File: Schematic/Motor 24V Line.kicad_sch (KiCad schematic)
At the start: 35 parts, among them Q31 CSD19531Q5A, Q32 CSD19531Q5A, U12 LM25190RGYR

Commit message: 1st Schematic Review
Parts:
- renumbered C137 to C140, C138 to C141, C139 to C142, C140 to C143, C141 to C144, C142 to C145, C143 to C146, C144 to C147, C145 to C148, C146 to C149, C147 to C150, C148 to C151, C149 to C152, C150 to C153, C151 to C154, C152 to C155, C153 to C156, C154 to C157, C155 to C158, C156 to C159, C157 to C160, C158 to C161, R129 to R131, R130 to R132, R131 to R133, R132 to R134, R133 to R135, R134 to R136, R135 to R137, R136 to R138, U12 to U15

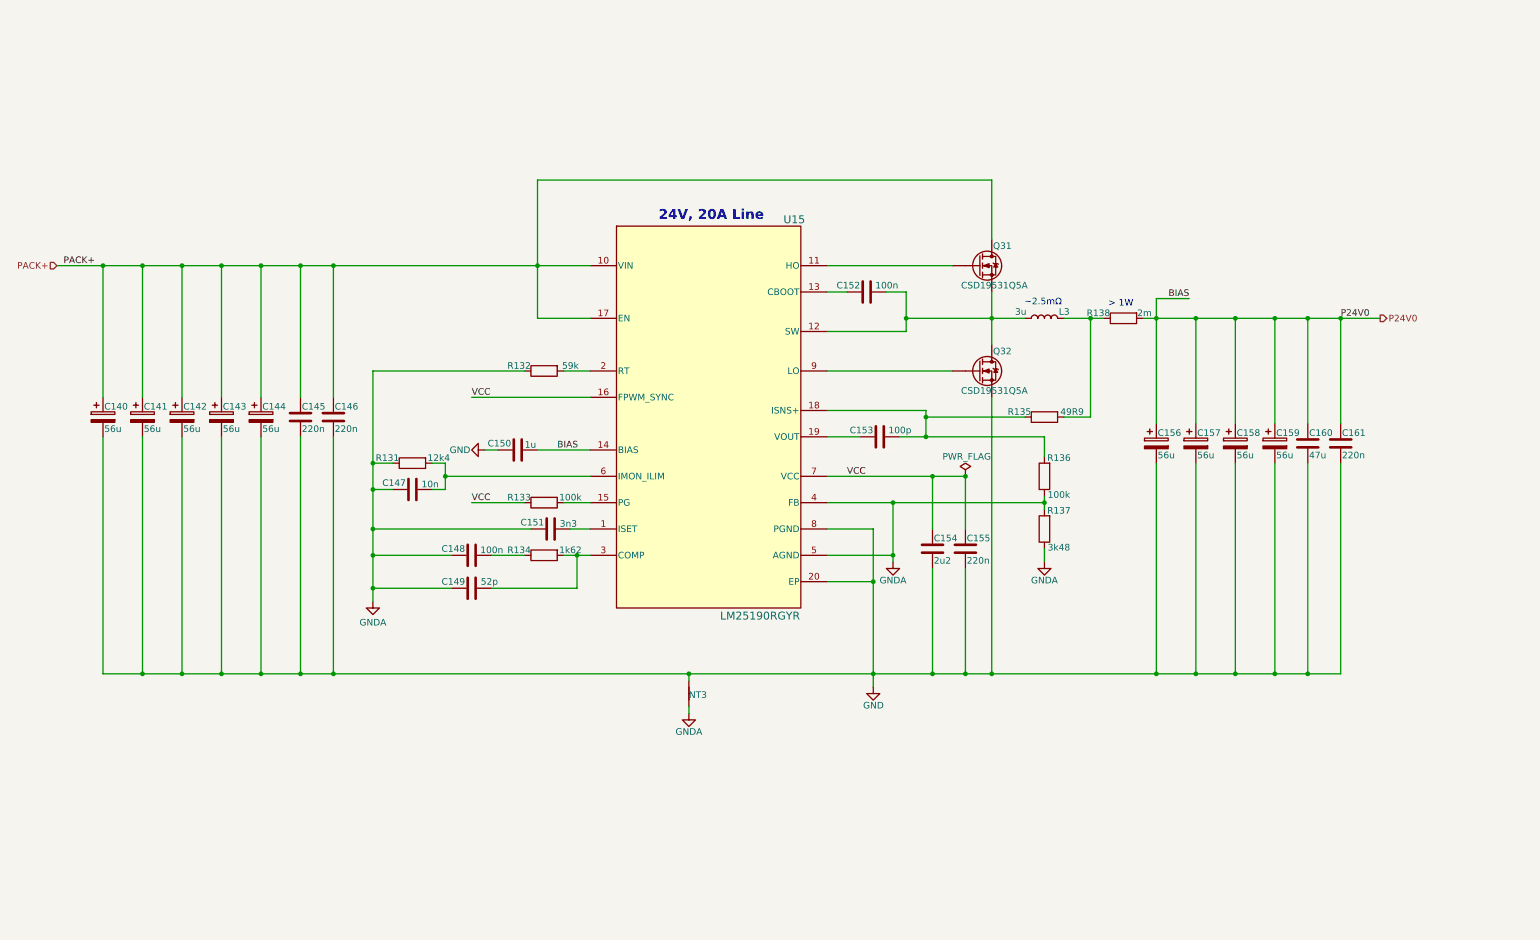
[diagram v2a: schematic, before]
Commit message: fixed power lines
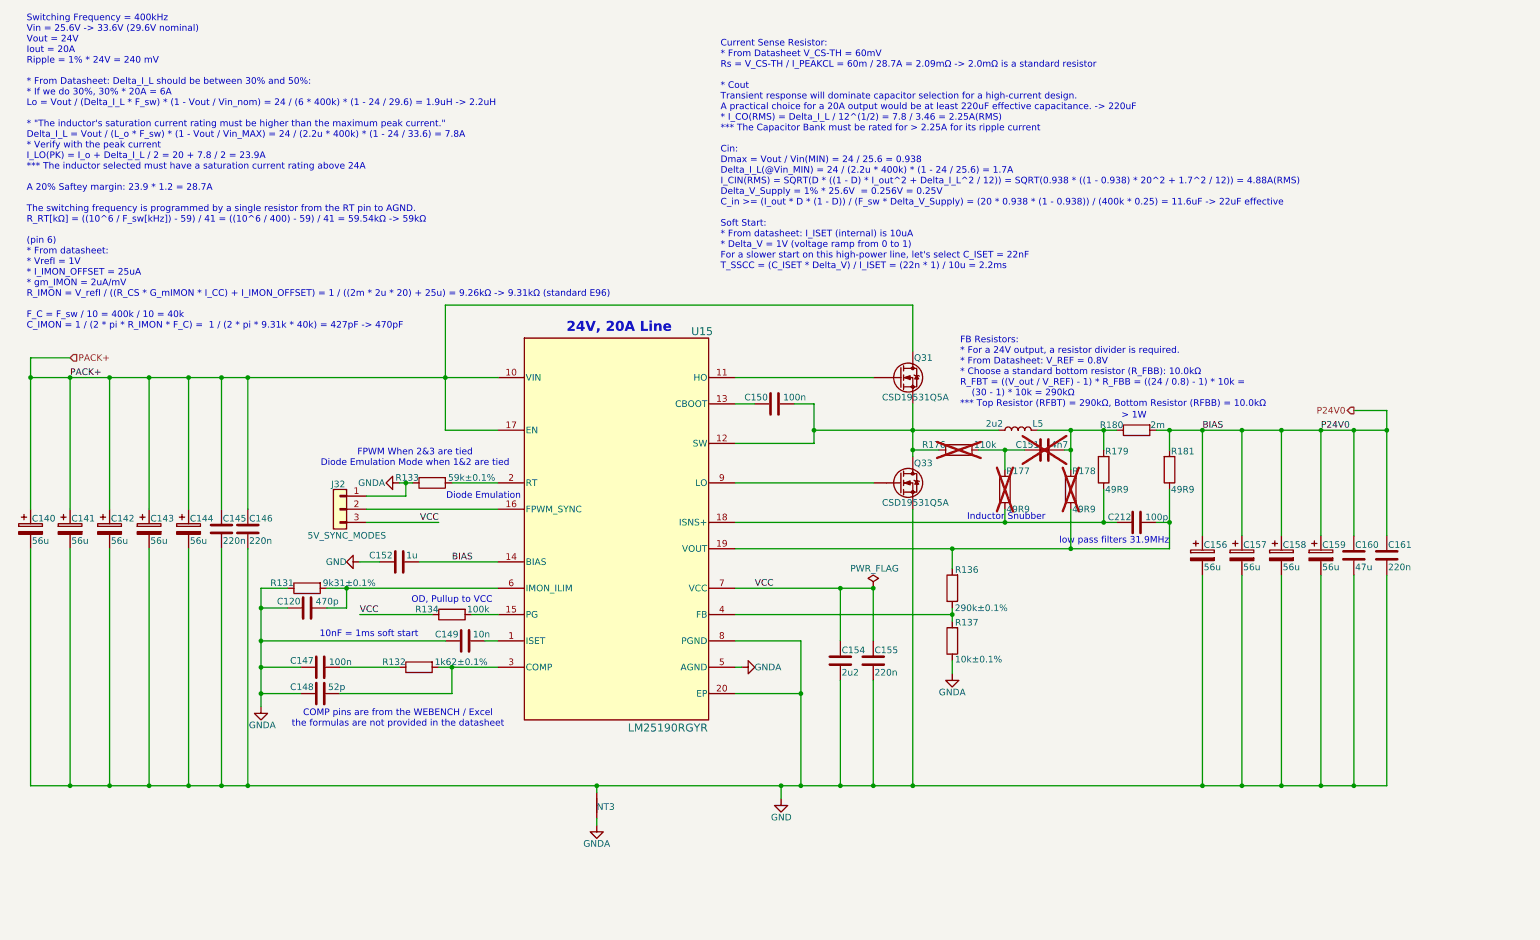
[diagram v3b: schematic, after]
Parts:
- removed C153: 100p, symbol Device:C
- removed L3: 3u, symbol Device:L
- removed Q32: CSD19531Q5A, Package_TO_SOT_SMD:TDSON-8-1, symbol Transistor_FET:CSD19531Q5A
- removed R135: 49R9, symbol Device:R
- removed R138: 2m, symbol Device:R
- added C120: 470p, symbol Device:C
- added C212: 100p, symbol Device:C
- added J32: 5V_SYNC_MODES, symbol Connector_Generic:Conn_01x03
- added L5: 2u2, symbol Device:L
- added Q33: CSD19531Q5A, Package_TO_SOT_SMD:TDSON-8-1, symbol Transistor_FET:CSD19531Q5A
- added R176: 110k, symbol Device:R
- added R177, R178, R179, R181: 49R9, symbol Device:R
- added R180: 2m, symbol Device:R
- C147: value 10n -> 100n
- C148: value 100n -> 52p
- C149: value 52p -> 10n
- C150: value 1u -> 100n
- C151: value 3n3 -> 4n7; now not fitted
- C152: value 100n -> 1u
- R131: value 12k4 -> 9k31±0.1%
- R132: value 59k -> 1k62±0.1%
- R133: value 100k -> 59k±0.1%
- R134: value 1k62 -> 100k
- R136: value 100k -> 290k±0.1%
- R137: value 3k48 -> 10k±0.1%
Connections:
- net GND: now also C152.1, Q33.1 (S), Q33.2 (S), Q33.3 (S); no longer C150.1
- net GNDA: now also R133.1, C120.1, J32.1 (Pin_1); no longer C151.1, R132.1, R136.1, R137.2, U15.4 (FB)
- net P24V0: now also C152.2, R180.2, R181.2; no longer C150.2
- net VCC: now also R134.1, J32.3 (Pin_3); no longer R133.1, U15.16 (FPWM_SYNC)
- net at Q31.1 (S), Q31.2 (S), Q31.3 (S)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: now also C150.2, L5.1, Q33.5 (D), R176.1; no longer C152.2
- net at U15.18 (ISNS+): now also C212.1, R177.1, R179.1; no longer R136.2
- net at C148.2: now also R132.2, U15.3 (COMP); no longer R134.1
- net at U15.19 (VOUT): now also R136.2, C212.2, R178.1, R181.1
- net at R133.2: now also U15.2 (RT); no longer U15.15 (PG)
- net at C151.2: now also L5.2, R178.2, R179.2, R180.1; no longer U15.1 (ISET)
- net at U15.13 (CBOOT): now also C150.1; no longer C152.1
- net at R131.2, U15.6 (IMON_ILIM): now also C120.2; no longer C147.2
- net at U15.9 (LO): now also Q33.4 (G)
- new net: C147.2, R132.1
- new net: C151.1, R176.2, R177.2
- new net: C149.2, U15.1 (ISET)
- new net: R134.2, U15.15 (PG)
- new net: J32.2 (Pin_2), U15.16 (FPWM_SYNC)
- new net: R136.1, R137.2, U15.4 (FB)
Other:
- note added: "10nF = 1ms soft start"
- note added: "COMP pins are from the WEBENCH / Excel the formulas are not provided in the datasheet"
- note added: "Current Sense Resistor: * From Datasheet V_CS-TH = 60mV Rs = V_CS-TH / I_PEAKCL = 60m / 28.7A = 2.09mΩ -> 2.0mΩ is a standard resistor * Cout Transient response will dominate capacitor selection for a high-current design. A practical choice for a 20A output would be at least 220uF effective capacitance. -> 220uF * I_CO(RMS) = Delta_I_L / 12^(1/2) = 7.8 / 3.46 = 2.25A(RMS) *** The Capacitor Bank m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"
- note added: "Diode Emulation"
- note added: "FB Resistors: * For a 24V output, a resistor divider is required. * From Datasheet: V_REF = 0.8V * Choose a standard bottom resistor (R_FBB): 10.0kΩ R_FBT = ((V_out / V_REF) - 1) * R_FBB = ((24 / 0.8) - 1) * 10k = (30 - 1) * 10k = 290kΩ *** Top Resistor (RFBT) = 290kΩ, Bottom Resistor (RFBB) = 10.0kΩ"
- note added: "FPWM When 2&3 are tied Diode Emulation Mode when 1&2 are tied"
- note added: "Inductor Snubber"
- note added: "OD, Pullup to VCC"
- note added: "Switching Frequency = 400kHz Vin = 25.6V -> 33.6V (29.6V nominal) Vout = 24V Iout = 20A Ripple = 1% * 24V = 240 mV * From Datasheet: Delta_I_L should be between 30% and 50%: * If we do 30%, 30% * 20A = 6A Lo = Vout / (Delta_I_L * F_sw) * (1 - Vout / Vin_nom) = 24 / (6 * 400k) * (1 - 24 / 29.6) = 1.9uH -> 2.2uH * "The inductor's saturation current rating must be higher than the maximum peak curren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"
- note added: "low pass filters 31.9MHz"
- note removed: "~2.5mΩ"
- moved on the sheet: C140, C141, C142, C143, C144, C145, C146, C154, C155, C156, C157, C158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

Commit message: updates
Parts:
- renumbered C140 to C141, C141 to C142, C142 to C143, C143 to C144, C144 to C145, C145 to C146, C146 to C147, C120 to C148, C147 to C149, C148 to C150, C152 to C151, C149 to C152, C150 to C153, C151 to C156, C212 to C157, C156 to C158, C157 to C159, C158 to C160, C159 to C161, C160 to C162, C161 to C163, J32 to J11, L5 to L3, Q33 to Q32, R131 to R140, R132 to R141, R133 to R142, R134 to R143, R136 to R144, R137 to R145, R176 to R146, R177 to R147, R178 to R148, R179 to R149, R180 to R150, R181 to R151
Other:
- note added: "using global GNDA, is this what we should be doing?"
- moved on the sheet: C147

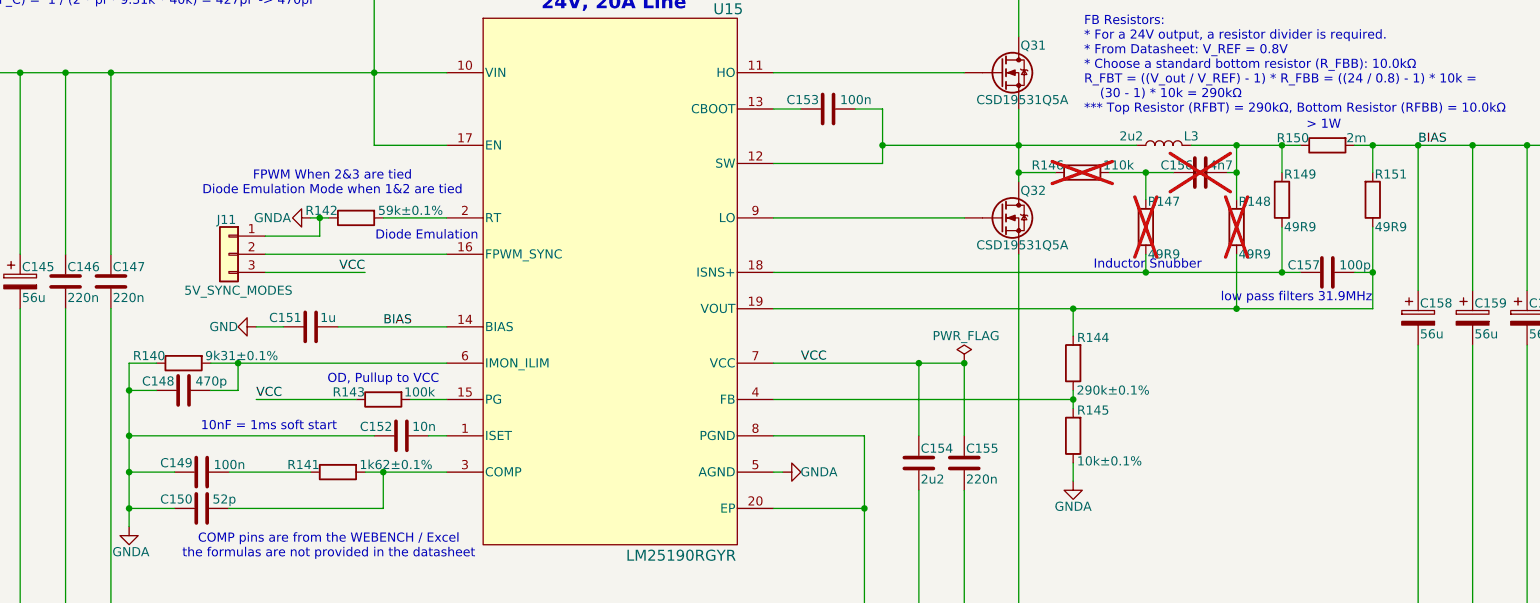
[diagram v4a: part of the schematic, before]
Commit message: updated fuel guage
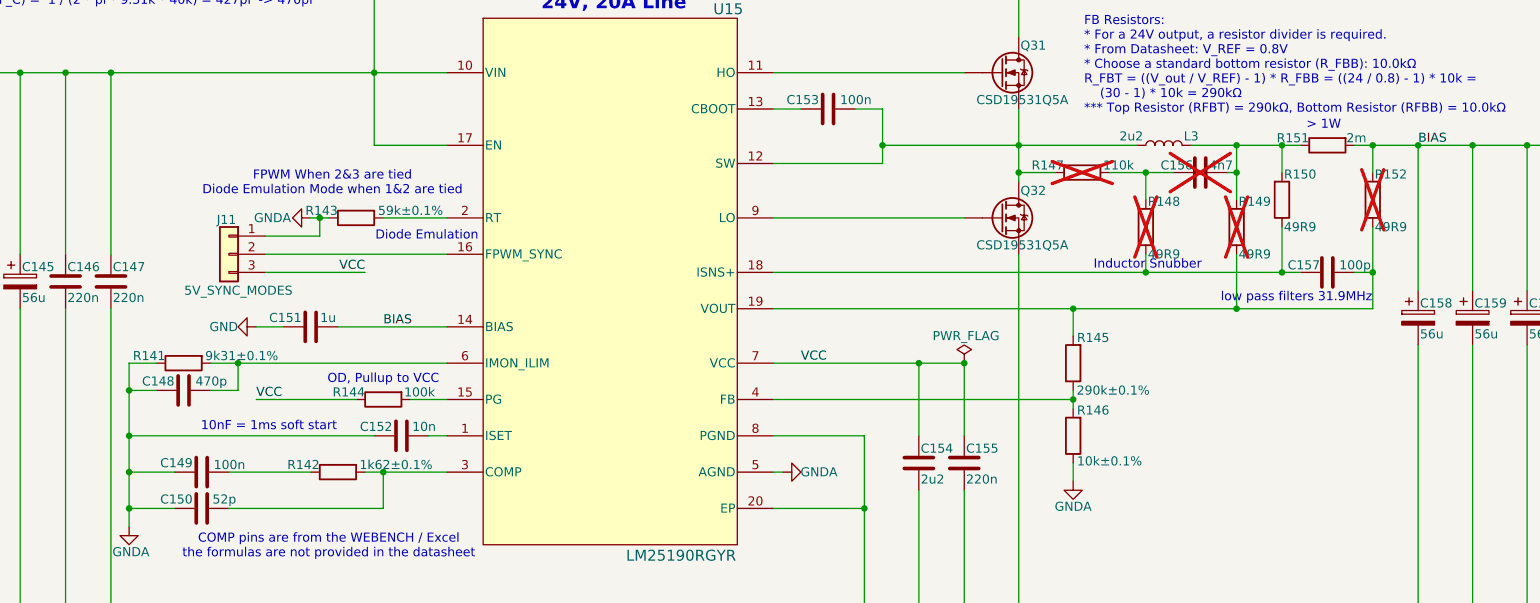
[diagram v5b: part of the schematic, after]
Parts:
- R152: renamed from R151; now not fitted
- renumbered R140 to R141, R141 to R142, R142 to R143, R143 to R144, R144 to R145, R145 to R146, R146 to R147, R147 to R148, R148 to R149, R149 to R150, R150 to R151
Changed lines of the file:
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@@
 		(on_board yes)
 		(dnp no)
-		(property "Reference" "R142"
+		(property "Reference" "R143"
 			(at 89.154 104.394 90)
 			(effects
@@
 			(project "STAR"
 				(path "/fc8533bc-25dd-4c20-9b4c-ffebebd6739b/f73d6367-f3ba-42df-a3ea-bd155f1c219f/3f0d1238-5e65-4d96-8961-a5c2e74dde4b"
-					(reference "R142")
+					(reference "R143")
 					(unit 1)
 				)
@@
 		(on_board yes)
 		(dnp yes)
-		(property "Reference" "R147"
+		(property "Reference" "R148"
 			(at 207.01 103.124 0)
 			(effects
@@
 			(project "STAR"
 				(path "/fc8533bc-25dd-4c20-9b4c-ffebebd6739b/f73d6367-f3ba-42df-a3ea-bd155f1c219f/3f0d1238-5e65-4d96-8961-a5c2e74dde4b"
-					(reference "R147")
+					(reference "R148")
 					(unit 1)
 				)
@@
 		(on_board yes)
 		(dnp no)
-		(property "Reference" "R141"
+		(property "Reference" "R142"
 			(at 86.614 139.954 90)
 			(effects
@@
 			(project "STAR"
 				(path "/fc8533bc-25dd-4c20-9b4c-ffebebd6739b/f73d6367-f3ba-42df-a3ea-bd155f1c219f/3f0d1238-5e65-4d96-8961-a5c2e74dde4b"
-					(reference "R141")
+					(reference "R142")
 					(unit 1)
 				)
@@
 		(in_bom yes)
 		(on_board yes)
-		(dnp no)
-		(property "Reference" "R151"
+		(dnp yes)
+		(property "Reference" "R152"
 			(at 238.76 99.314 0)
 			(effects
@@
 			(project "STAR"
 				(path "/fc8533bc-25dd-4c20-9b4c-ffebebd6739b/f73d6367-f3ba-42df-a3ea-bd155f1c219f/3f0d1238-5e65-4d96-8961-a5c2e74dde4b"
-					(reference "R151")
+					(reference "R152")
 					(unit 1)
 				)
@@
 		(on_board yes)
 		(dnp no)
-		(property "Reference" "R140"
+		(property "Reference" "R141"
 			(at 65.024 124.714 90)
 			(effects
@@
 			(project "STAR"
 				(path "/fc8533bc-25dd-4c20-9b4c-ffebebd6739b/f73d6367-f3ba-42df-a3ea-bd155f1c219f/3f0d1238-5e65-4d96-8961-a5c2e74dde4b"
-					(reference "R140")
+					(reference "R141")
 					(unit 1)
 				)
@@
 		(on_board yes)
 		(dnp no)
-		(property "Reference" "R144"
+		(property "Reference" "R145"
 			(at 197.104 122.174 0)
 			(effects
@@
 			(project "STAR"
 				(path "/fc8533bc-25dd-4c20-9b4c-ffebebd6739b/f73d6367-f3ba-42df-a3ea-bd155f1c219f/3f0d1238-5e65-4d96-8961-a5c2e74dde4b"
-					(reference "R144")
+					(reference "R145")
 					(unit 1)
 				)
@@
 		(on_board yes)
 		(dnp no)
-		(property "Reference" "R145"
+		(property "Reference" "R146"
 			(at 197.104 132.334 0)
 			(effects
@@
 			(project "STAR"
 				(path "/fc8533bc-25dd-4c20-9b4c-ffebebd6739b/f73d6367-f3ba-42df-a3ea-bd155f1c219f/3f0d1238-5e65-4d96-8961-a5c2e74dde4b"
-					(reference "R145")
+					(reference "R146")
 					(unit 1)
 				)
@@
 		(on_board yes)
 		(dnp no)
-		(property "Reference" "R149"
+		(property "Reference" "R150"
 			(at 226.06 99.314 0)
 			(effects
@@
 			(project "STAR"
 				(path "/fc8533bc-25dd-4c20-9b4c-ffebebd6739b/f73d6367-f3ba-42df-a3ea-bd155f1c219f/3f0d1238-5e65-4d96-8961-a5c2e74dde4b"
-					(reference "R149")
+					(reference "R150")
 					(unit 1)
 				)
@@
 		(on_board yes)
 		(dnp no)
-		(property "Reference" "R150"
+		(property "Reference" "R151"
 			(at 225.044 94.234 90)
 			(effects
@@
 			(project "STAR"
 				(path "/fc8533bc-25dd-4c20-9b4c-ffebebd6739b/f73d6367-f3ba-42df-a3ea-bd155f1c219f/3f0d1238-5e65-4d96-8961-a5c2e74dde4b"
-					(reference "R150")
+					(reference "R151")
 					(unit 1)
 				)
@@
 		(on_board yes)
 		(dnp yes)
-		(property "Reference" "R146"
+		(property "Reference" "R147"
 			(at 190.754 98.044 90)
 			(effects
@@
 			(project "STAR"
 				(path "/fc8533bc-25dd-4c20-9b4c-ffebebd6739b/f73d6367-f3ba-42df-a3ea-bd155f1c219f/3f0d1238-5e65-4d96-8961-a5c2e74dde4b"
-					(reference "R146")
+					(reference "R147")
 					(unit 1)
 				)
@@
 		(on_board yes)
 		(dnp yes)
-		(property "Reference" "R148"
+		(property "Reference" "R149"
 			(at 219.71 103.124 0)
 			(effects
@@
 			(project "STAR"
 				(path "/fc8533bc-25dd-4c20-9b4c-ffebebd6739b/f73d6367-f3ba-42df-a3ea-bd155f1c219f/3f0d1238-5e65-4d96-8961-a5c2e74dde4b"
-					(reference "R148")
+					(reference "R149")
 					(unit 1)
 				)
@@
 		(on_board yes)
 		(dnp no)
-		(property "Reference" "R143"
+		(property "Reference" "R144"
 			(at 92.964 129.794 90)
 			(effects
@@
 			(project "STAR"
 				(path "/fc8533bc-25dd-4c20-9b4c-ffebebd6739b/f73d6367-f3ba-42df-a3ea-bd155f1c219f/3f0d1238-5e65-4d96-8961-a5c2e74dde4b"
-					(reference "R143")
+					(reference "R144")
 					(unit 1)
 				)
